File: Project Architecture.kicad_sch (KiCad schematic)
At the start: 0 parts

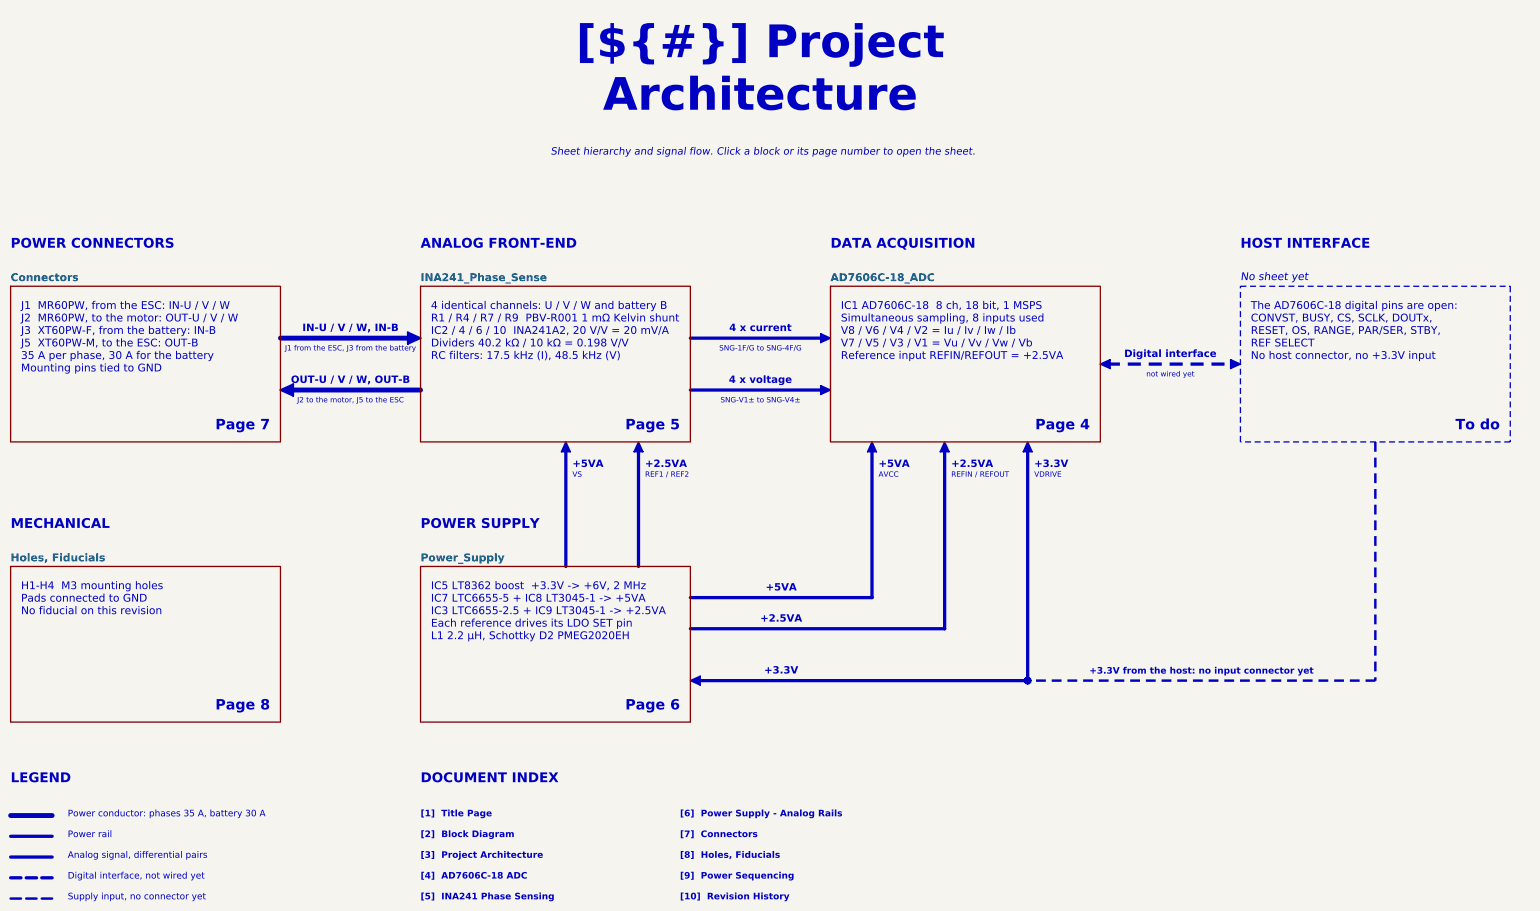
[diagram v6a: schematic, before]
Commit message: Restyle schematic sheets, new title block logo, WE-MAPI inductor in simulations
- Schematic sheets: restyled frames, tables and text boxes
- Title block: INGENIERIE FRANCE logo in KDT_Template_GIT.kicad_wks
- LTspice: L1 modelled as WE-MAPI 4030 74438357022 (22 mOhm),
  simulations 01 and 03 rerun, README and results updated

Co-Authored-By: Claude Opus 5.5 <noreply@anthropic.com>
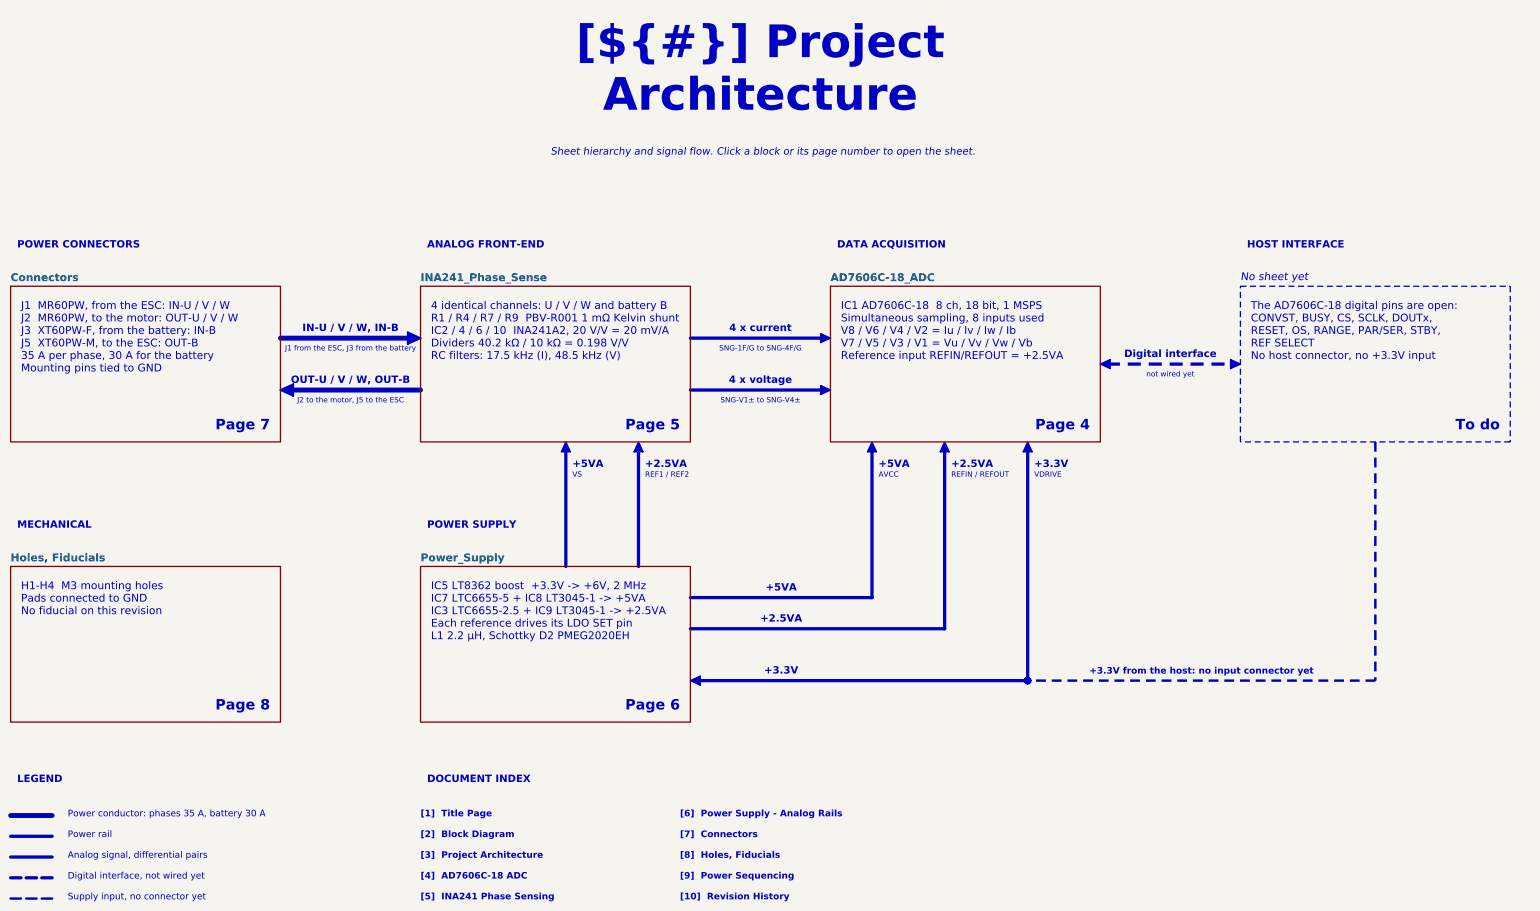
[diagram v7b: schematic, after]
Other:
- note removed: "ANALOG FRONT-END"
- note removed: "DATA ACQUISITION"
- note removed: "DOCUMENT INDEX"
- note removed: "HOST INTERFACE"
- note removed: "LEGEND"
- note removed: "MECHANICAL"
- note removed: "POWER CONNECTORS"
- note removed: "POWER SUPPLY"
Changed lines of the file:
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@@
-		)
-	)
-	(text "DATA ACQUISITION"
-		(exclude_from_sim no)
-		(at 227.33 72.39 0)
-		(effects
-			(font
-				(face "Arial")
-				(size 2.4 2.4)
-				(bold yes)
-				(color 111 84 181 1)
-			)
-			(justify left bottom)
 		)
 	)
@@
 		)
 	)
-	(text "POWER SUPPLY"
-		(exclude_from_sim no)
-		(at 127 140.97 0)
-		(effects
-			(font
-				(face "Arial")
-				(size 2.4 2.4)
-				(bold yes)
-				(color 176 64 102 1)
-			)
-			(justify left bottom)
-		)
-	)
 	(text "AVCC"
 		(exclude_from_sim no)
@@
 			)
 			(justify top)
-		)
-	)
-	(text "MECHANICAL"
-		(exclude_from_sim no)
-		(at 26.67 140.97 0)
-		(effects
-			(font
-				(face "Arial")
-				(size 2.4 2.4)
-				(bold yes)
-				(color 120 120 120 1)
-			)
-			(justify left bottom)
 		)
 	)
@@
 		)
 	)
-	(text "HOST INTERFACE"
-		(exclude_from_sim no)
-		(at 327.66 72.39 0)
-		(effects
-			(font
-				(face "Arial")
-				(size 2.4 2.4)
-				(bold yes)
-				(color 120 120 120 1)
-			)
-			(justify left bottom)
-		)
-	)
 	(text "[1]  Title Page"
 		(exclude_from_sim no)
@@
 		)
 	)
-	(text "LEGEND"
-		(exclude_from_sim no)
-		(at 26.67 203.2 0)
-		(effects
-			(font
-				(face "Arial")
-				(size 2.4 2.4)
-				(bold yes)
-				(color 40 40 40 1)
-			)
-			(justify left bottom)
-		)
-	)
 	(text "+2.5VA"
 		(exclude_from_sim no)
@@
 			)
 			(justify bottom)
-		)
-	)
-	(text "ANALOG FRONT-END"
-		(exclude_from_sim no)
-		(at 127 72.39 0)
-		(effects
-			(font
-				(face "Arial")
-				(size 2.4 2.4)
-				(bold yes)
-				(color 21 128 61 1)
-			)
-			(justify left bottom)
-		)
-	)
-	(text "POWER CONNECTORS"
-		(exclude_from_sim no)
-		(at 26.67 72.39 0)
-		(effects
-			(font
-				(face "Arial")
-				(size 2.4 2.4)
-				(bold yes)
-				(color 74 155 203 1)
-			)
-			(justify left bottom)
-		)
-	)
-	(text "DOCUMENT INDEX"
-		(exclude_from_sim no)
-		(at 127 203.2 0)
-		(effects
-			(font
-				(face "Arial")
-				(size 2.4 2.4)
-				(bold yes)
-				(color 40 40 40 1)
-			)
-			(justify left bottom)
 		)
 	)
@@
 		)
 	)
+	(text_box "POWER CONNECTORS"
+		(exclude_from_sim no)
+		(at 26.67 67.79 0)
+		(size 66.04 6.35)
+		(margins 1.6 1.6 1.6 1.6)
+		(stroke
+			(width -0.0001)
+			(type solid)
+		)
+		(fill
+			(type color)
+			(color 74 155 203 1)
+		)
+		(effects
+			(font
+				(face "Arial")
+				(size 1.8 1.8)
+				(thickness 0.36)
+				(bold yes)
+				(color 255 255 255 1)
+			)
+			(justify left)
+		)
+	)
+	(text_box "ANALOG FRONT-END"
+		(exclude_from_sim no)
+		(at 127 67.79 0)
+		(size 66.04 6.35)
+		(margins 1.6 1.6 1.6 1.6)
+		(stroke
+			(width -0.0001)
+			(type solid)
+		)
+		(fill
+			(type color)
+			(color 21 128 61 1)
+		)
+		(effects
+			(font
+				(face "Arial")
+				(size 1.8 1.8)
+				(thickness 0.36)
+				(bold yes)
+				(color 255 255 255 1)
+			)
+			(justify left)
+		)
+	)
+	(text_box "DATA ACQUISITION"
+		(exclude_from_sim no)
+		(at 227.33 67.79 0)
+		(size 66.04 6.35)
+		(margins 1.6 1.6 1.6 1.6)
+		(stroke
+			(width -0.0001)
+			(type solid)
+		)
+		(fill
+			(type color)
+			(color 111 84 181 1)
+		)
+		(effects
+			(font
+				(face "Arial")
+				(size 1.8 1.8)
+				(thickness 0.36)
+				(bold yes)
+				(color 255 255 255 1)
+			)
+			(justify left)
+		)
+	)
+	(text_box "HOST INTERFACE"
+		(exclude_from_sim no)
+		(at 327.66 67.79 0)
+		(size 66.04 6.35)
+		(margins 1.6 1.6 1.6 1.6)
+		(stroke
+			(width -0.0001)
+			(type solid)
+		)
+		(fill
+			(type color)
+			(color 120 120 120 1)
+		)
+		(effects
+			(font
+				(face "Arial")
+				(size 1.8 1.8)
+				(thickness 0.36)
+				(bold yes)
+				(color 255 255 255 1)
+			)
+			(justify left)
+		)
+	)
+	(text_box "MECHANICAL"
+		(exclude_from_sim no)
+		(at 26.67 136.37 0)
+		(size 66.04 6.35)
+		(margins 1.6 1.6 1.6 1.6)
+		(stroke
+			(width -0.0001)
+			(type solid)
+		)
+		(fill
+			(type color)
+			(color 120 120 120 1)
+		)
+		(effects
+			(font
+				(face "Arial")
+				(size 1.8 1.8)
+				(thickness 0.36)
+				(bold yes)
+				(color 255 255 255 1)
+			)
+			(justify left)
+		)
+	)
+	(text_box "POWER SUPPLY"
+		(exclude_from_sim no)
+		(at 127 136.37 0)
+		(size 66.04 6.35)
+		(margins 1.6 1.6 1.6 1.6)
+		(stroke
+			(width -0.0001)
+			(type solid)
+		)
+		(fill
+			(type color)
+			(color 176 64 102 1)
+		)
+		(effects
+			(font
+				(face "Arial")
+				(size 1.8 1.8)
+				(thickness 0.36)
+				(bold yes)
+				(color 255 255 255 1)
+			)
+			(justify left)
+		)
+	)
+	(text_box "LEGEND"
+		(exclude_from_sim no)
+		(at 26.67 198.6 0)
+		(size 85.09 6.35)
+		(margins 1.6 1.6 1.6 1.6)
+		(stroke
+			(width -0.0001)
+			(type solid)
+		)
+		(fill
+			(type color)
+			(color 70 70 70 1)
+		)
+		(effects
+			(font
+				(face "Arial")
+				(size 1.8 1.8)
+				(thickness 0.36)
+				(bold yes)
+				(color 255 255 255 1)
+			)
+			(justify left)
+		)
+	)
+	(text_box "DOCUMENT INDEX"
+		(exclude_from_sim no)
+		(at 127 198.6 0)
+		(size 101.6 6.35)
+		(margins 1.6 1.6 1.6 1.6)
+		(stroke
+			(width -0.0001)
+			(type solid)
+		)
+		(fill
+			(type color)
+			(color 70 70 70 1)
+		)
+		(effects
+			(font
+				(face "Arial")
+				(size 1.8 1.8)
+				(thickness 0.36)
+				(bold yes)
+				(color 255 255 255 1)
+			)
+			(justify left)
+		)
+	)

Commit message: Wire the AD7606C-18 digital side to host header J4, add test points
- AD7606C-18: software mode (OS0-2 high), serial (PAR/SER SEL high),
  REF SELECT low; CONVST, BUSY, RESET, CS, SCLK, SDI, FRSTDATA and
  DOUTA-D to J4 (2x8 pin header 2.54 mm, horizontal), +3.3V on J4 pin 1
- AD7606C-18 AGND pin 26 and REFGND pin 46 on GND
- Test points TP1-TP16: rails, INA241 outputs, CONVST, BUSY
- Nets renamed SHUNT_*, INA_*, ADC_*; net colours in the project
- LT3045-1 footprint: thermal vias numbered as exposed pad 13
- PCB updated from the schematic; ADC_* digital nets not routed yet
- README template / CHANGELOG: status, J4 pinout, design review 1 and 2
  fixed, new finding 9 (VDRIVE above AVCC + 0.3 V at power-up),
  4 channels / 8 ADC inputs

Co-Authored-By: Claude Opus 5.5 <noreply@anthropic.com>
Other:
- note added: "+3.3V from the host, J4 pin 1"
- note added: "ADC_U_I± to ADC_BAT_I±"
- note added: "ADC_U_V± to ADC_BAT_V±"
- note added: "Connectors, J4"
- note added: "Digital interface (J4)"
- note added: "J4, 2x8 Dupont header to the host: +3.3V, GND, CONVST, BUSY, CS, SCLK, SDI, DOUTA-D, RESET, FRSTDATA AD7606C-18 in software mode, serial interface"
- note added: "SPI, 4 DOUT lines"
- note added: "Supply input from the host (J4)"
- note removed: "+3.3V from the host: no input connector yet"
- note removed: "Digital interface, not wired yet"
- note removed: "No sheet yet"
- note removed: "SNG-1F/G to SNG-4F/G"
- note removed: "SNG-V1± to SNG-V4±"
- note removed: "Supply input, no connector yet"
- note removed: "The AD7606C-18 digital pins are open: CONVST, BUSY, CS, SCLK, DOUTx, RESET, OS, RANGE, PAR/SER, STBY, REF SELECT No host connector, no +3.3V input"
- note removed: "To do"
- note removed: "not wired yet"
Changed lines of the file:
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@@
 		)
 	)
-	(text "not wired yet"
+	(text "SPI, 4 DOUT lines"
 		(exclude_from_sim no)
 		(at 310.515 102.23 0)
@@
 		)
 	)
-	(text "SNG-V1± to SNG-V4±"
+	(text "ADC_U_V± to ADC_BAT_V±"
 		(exclude_from_sim no)
 		(at 210.185 108.58 0)
@@
 		)
 	)
-	(text "SNG-1F/G to SNG-4F/G"
+	(text "ADC_U_I± to ADC_BAT_I±"
 		(exclude_from_sim no)
 		(at 210.185 95.88 0)
@@
 		)
 	)
-	(text "+3.3V from the host: no input connector yet"
+	(text "+3.3V from the host, J4 pin 1"
 		(exclude_from_sim no)
 		(at 318.135 176.53 0)
@@
 		)
 	)
-	(text "Supply input, no connector yet"
+	(text "Supply input from the host (J4)"
 		(exclude_from_sim no)
 		(at 40.64 231.775 0)
@@
 		)
 	)
-	(text "To do"
+	(text "Page 7"
 		(exclude_from_sim no)
 		(at 391.16 116.84 0)
@@
 		)
 	)
-	(text "Digital interface, not wired yet"
+	(text "Digital interface (J4)"
 		(exclude_from_sim no)
 		(at 40.64 226.695 0)
@@
 		)
 	)
-	(text "No sheet yet"
+	(text "Connectors, J4"
 		(exclude_from_sim no)
 		(at 327.66 80.2509 0)
@@
 		)
 	)
-	(text "The AD7606C-18 digital pins are open:\nCONVST, BUSY, CS, SCLK, DOUTx,\nRESET, OS, RANGE, PAR/SER, STBY,\nREF SELECT\nNo host connector, no +3.3V input"
+	(text "J4, 2x8 Dupont header to the host:\n+3.3V, GND, CONVST, BUSY, CS, SCLK,\nSDI, DOUTA-D, RESET, FRSTDATA\nAD7606C-18 in software mode,\nserial interface"
 		(exclude_from_sim no)
 		(at 330.2 85.09 0)
@@
 			)
 			(justify left top)
+		)
+	)
+	(text_box "DATA ACQUISITION"
+		(exclude_from_sim no)
+		(at 227.33 67.79 0)
+		(size 66.04 6.35)
+		(margins 1.6 1.6 1.6 1.6)
+		(stroke
+			(width -0.0001)
+			(type solid)
+		)
+		(fill
+			(type color)
+			(color 111 84 181 1)
+		)
+		(effects
+			(font
+				(face "Arial")
+				(size 1.8 1.8)
+				(thickness 0.36)
+				(bold yes)
+				(color 255 255 255 1)
+			)
+			(justify left)
+		)
+	)
+	(text_box "LEGEND"
+		(exclude_from_sim no)
+		(at 26.67 198.6 0)
+		(size 85.09 6.35)
+		(margins 1.6 1.6 1.6 1.6)
+		(stroke
+			(width -0.0001)
+			(type solid)
+		)
+		(fill
+			(type color)
+			(color 70 70 70 1)
+		)
+		(effects
+			(font
+				(face "Arial")
+				(size 1.8 1.8)
+				(thickness 0.36)
+				(bold yes)
+				(color 255 255 255 1)
+			)
+			(justify left)
+		)
+	)
+	(text_box "MECHANICAL"
+		(exclude_from_sim no)
+		(at 26.67 136.37 0)
+		(size 66.04 6.35)
+		(margins 1.6 1.6 1.6 1.6)
+		(stroke
+			(width -0.0001)
+			(type solid)
+		)
+		(fill
+			(type color)
+			(color 120 120 120 1)
+		)
+		(effects
+			(font
+				(face "Arial")
+				(size 1.8 1.8)
+				(thickness 0.36)
+				(bold yes)
+				(color 255 255 255 1)
+			)
+			(justify left)
+		)
+	)
+	(text_box "ANALOG FRONT-END"
+		(exclude_from_sim no)
+		(at 127 67.79 0)
+		(size 66.04 6.35)
+		(margins 1.6 1.6 1.6 1.6)
+		(stroke
+			(width -0.0001)
+			(type solid)
+		)
+		(fill
+			(type color)
+			(color 21 128 61 1)
+		)
+		(effects
+			(font
+				(face "Arial")
+				(size 1.8 1.8)
+				(thickness 0.36)
+				(bold yes)
+				(color 255 255 255 1)
+			)
+			(justify left)
+		)
+	)
+	(text_box "POWER SUPPLY"
+		(exclude_from_sim no)
+		(at 127 136.37 0)
+		(size 66.04 6.35)
+		(margins 1.6 1.6 1.6 1.6)
+		(stroke
+			(width -0.0001)
+			(type solid)
+		)
+		(fill
+			(type color)
+			(color 176 64 102 1)
+		)
+		(effects
+			(font
+				(face "Arial")
+				(size 1.8 1.8)
+				(thickness 0.36)
+				(bold yes)
+				(color 255 255 255 1)
+			)
+			(justify left)
+		)
+	)
+	(text_box "POWER CONNECTORS"
+		(exclude_from_sim no)
+		(at 26.67 67.79 0)
+		(size 66.04 6.35)
+		(margins 1.6 1.6 1.6 1.6)
+		(stroke
+			(width -0.0001)
+			(type solid)
+		)
+		(fill
+			(type color)
+			(color 74 155 203 1)
+		)
+		(effects
+			(font
+				(face "Arial")
+				(size 1.8 1.8)
+				(thickness 0.36)
+				(bold yes)
+				(color 255 255 255 1)
+			)
+			(justify left)
+		)
+	)
+	(text_box "DOCUMENT INDEX"
+		(exclude_from_sim no)
+		(at 127 198.6 0)
+		(size 101.6 6.35)
+		(margins 1.6 1.6 1.6 1.6)
+		(stroke
+			(width -0.0001)
+			(type solid)
+		)
+		(fill
+			(type color)
+			(color 70 70 70 1)
+		)
+		(effects
+			(font
+				(face "Arial")
+				(size 1.8 1.8)
+				(thickness 0.36)
+				(bold yes)
+				(color 255 255 255 1)
+			)
+			(justify left)
+		)
+	)
+	(text_box "HOST INTERFACE"
+		(exclude_from_sim no)
+		(at 327.66 67.79 0)
+		(size 66.04 6.35)
+		(margins 1.6 1.6 1.6 1.6)
+		(stroke
+			(width -0.0001)
+			(type solid)
+		)
+		(fill
+			(type color)
+			(color 120 120 120 1)
+		)
+		(effects
+			(font
+				(face "Arial")
+				(size 1.8 1.8)
+				(thickness 0.36)
+				(bold yes)
+				(color 255 255 255 1)
+			)
+			(justify left)
 		)
 	)
@@
 		)
 	)
-	(text_box "POWER CONNECTORS"
-		(exclude_from_sim no)
-		(at 26.67 67.79 0)
-		(size 66.04 6.35)
-		(margins 1.6 1.6 1.6 1.6)
-		(stroke
-			(width -0.0001)
-			(type solid)
-		)
-		(fill
-			(type color)
-			(color 74 155 203 1)
-		)
-		(effects
-			(font
-				(face "Arial")
-				(size 1.8 1.8)
-				(thickness 0.36)
-				(bold yes)
-				(color 255 255 255 1)
-			)
-			(justify left)
-		)
-	)
-	(text_box "ANALOG FRONT-END"
-		(exclude_from_sim no)
-		(at 127 67.79 0)
-		(size 66.04 6.35)
-		(margins 1.6 1.6 1.6 1.6)
-		(stroke
-			(width -0.0001)
-			(type solid)
-		)
-		(fill
-			(type color)
-			(color 21 128 61 1)
-		)
-		(effects
-			(font
-				(face "Arial")
-				(size 1.8 1.8)
-				(thickness 0.36)
-				(bold yes)
-				(color 255 255 255 1)
-			)
-			(justify left)
-		)
-	)
-	(text_box "DATA ACQUISITION"
-		(exclude_from_sim no)
-		(at 227.33 67.79 0)
-		(size 66.04 6.35)
-		(margins 1.6 1.6 1.6 1.6)
-		(stroke
-			(width -0.0001)
-			(type solid)
-		)
-		(fill
-			(type color)
-			(color 111 84 181 1)
-		)
-		(effects
-			(font
-				(face "Arial")
-				(size 1.8 1.8)
-				(thickness 0.36)
-				(bold yes)
-				(color 255 255 255 1)
-			)
-			(justify left)
-		)
-	)
-	(text_box "HOST INTERFACE"
-		(exclude_from_sim no)
-		(at 327.66 67.79 0)
-		(size 66.04 6.35)
-		(margins 1.6 1.6 1.6 1.6)
-		(stroke
-			(width -0.0001)
-			(type solid)
-		)
-		(fill
-			(type color)
-			(color 120 120 120 1)
-		)
-		(effects
-			(font
-				(face "Arial")
-				(size 1.8 1.8)
-				(thickness 0.36)
-				(bold yes)
-				(color 255 255 255 1)
-			)
-			(justify left)
-		)
-	)
-	(text_box "MECHANICAL"
-		(exclude_from_sim no)
-		(at 26.67 136.37 0)
-		(size 66.04 6.35)
-		(margins 1.6 1.6 1.6 1.6)
-		(stroke
-			(width -0.0001)
-			(type solid)
-		)
-		(fill
-			(type color)
-			(color 120 120 120 1)
-		)
-		(effects
-			(font
-				(face "Arial")
-				(size 1.8 1.8)
-				(thickness 0.36)
-				(bold yes)
-				(color 255 255 255 1)
-			)
-			(justify left)
-		)
-	)
-	(text_box "POWER SUPPLY"
-		(exclude_from_sim no)
-		(at 127 136.37 0)
-		(size 66.04 6.35)
-		(margins 1.6 1.6 1.6 1.6)
-		(stroke
-			(width -0.0001)
-			(type solid)
-		)
-		(fill
-			(type color)
-			(color 176 64 102 1)
-		)
-		(effects
-			(font
-				(face "Arial")
-				(size 1.8 1.8)
-				(thickness 0.36)
-				(bold yes)
-				(color 255 255 255 1)
-			)
-			(justify left)
-		)
-	)
-	(text_box "LEGEND"
-		(exclude_from_sim no)
-		(at 26.67 198.6 0)
-		(size 85.09 6.35)
-		(margins 1.6 1.6 1.6 1.6)
-		(stroke
-			(width -0.0001)
-			(type solid)
-		)
-		(fill
-			(type color)
-			(color 70 70 70 1)
-		)
-		(effects
-			(font
-				(face "Arial")
-				(size 1.8 1.8)
-				(thickness 0.36)
-				(bold yes)
-				(color 255 255 255 1)
-			)
-			(justify left)
-		)
-	)
-	(text_box "DOCUMENT INDEX"
-		(exclude_from_sim no)
-		(at 127 198.6 0)
-		(size 101.6 6.35)
-		(margins 1.6 1.6 1.6 1.6)
-		(stroke
-			(width -0.0001)
-			(type solid)
-		)
-		(fill
-			(type color)
-			(color 70 70 70 1)
-		)
-		(effects
-			(font
-				(face "Arial")
-				(size 1.8 1.8)
-				(thickness 0.36)
-				(bold yes)
-				(color 255 255 255 1)
-			)
-			(justify left)
-		)
-	)
